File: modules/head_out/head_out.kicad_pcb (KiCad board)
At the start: 2 copper layers, 30.5 x 68.6 mm, 28 parts, among them U1 MCP6002-xSN

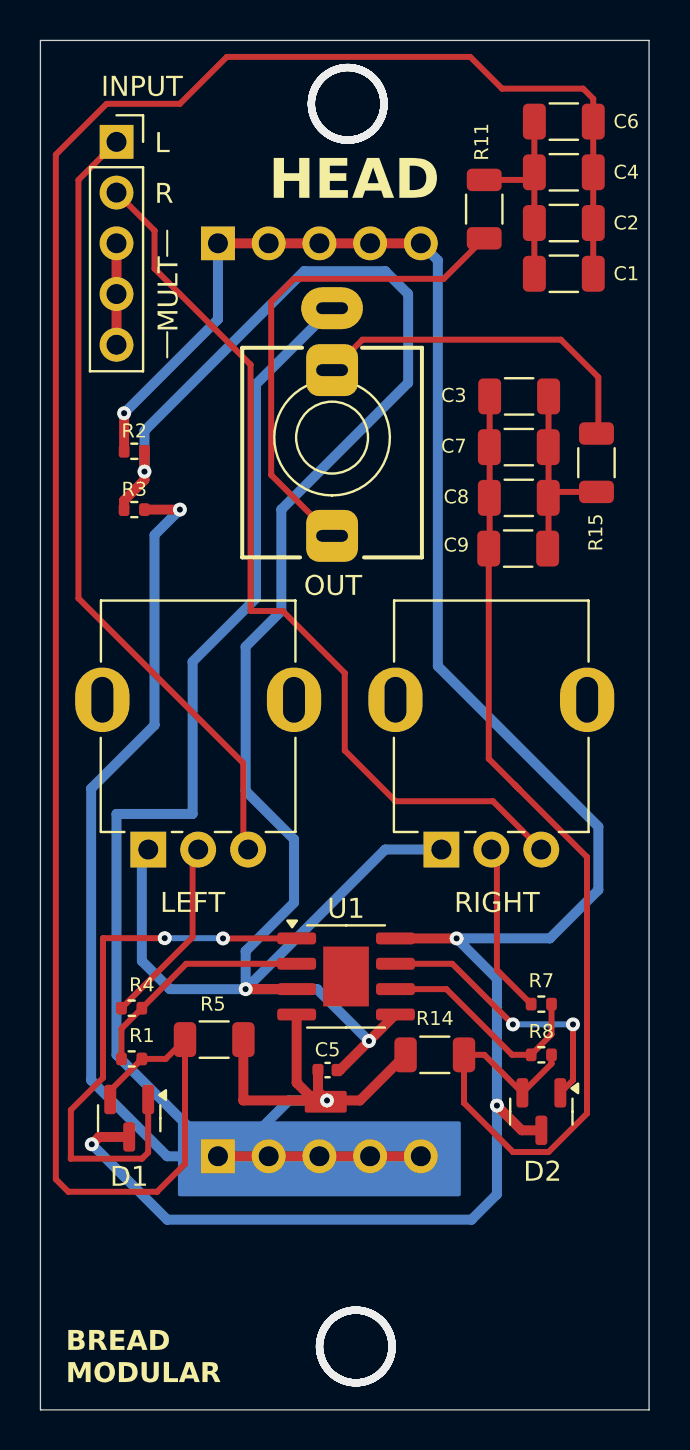
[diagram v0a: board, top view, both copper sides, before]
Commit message: head_out: Add more volume to support larger headphones. Now we offer more volume and removed the transistor. The opamp can handle the power requirment decently.
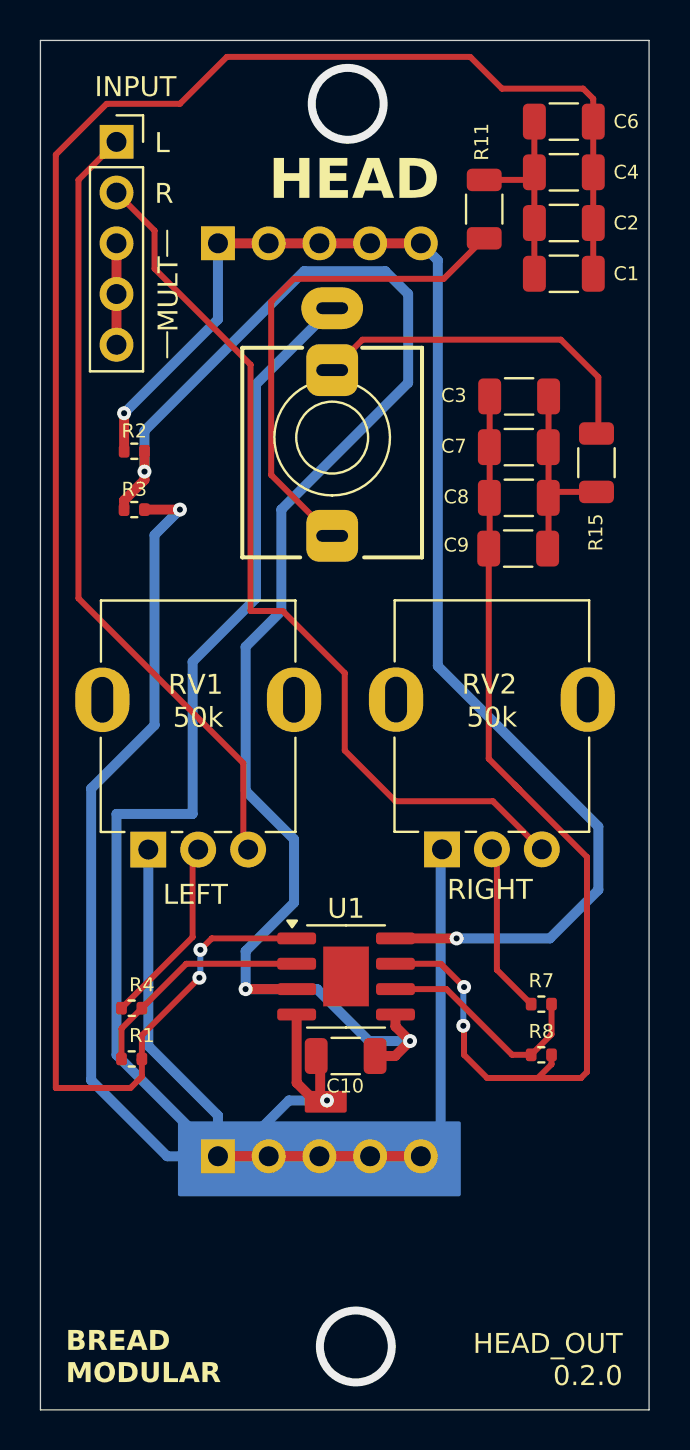
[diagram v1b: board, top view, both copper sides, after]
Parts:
- removed C5: 0.1uf, Capacitor_SMD:C_0402_1005Metric
- removed D1, D2: SS8050, Package_TO_SOT_SMD:SOT-23
- removed INPUT: Conn_01x05_Socket, Connector_PinSocket_2.54mm:PinSocket_1x05_P2.54mm_Vertical
- removed LEFT, RIGHT: 50k, BreadModular_Pots:Potentiometer_RV09
- removed OUT: AudioJack3, BreadModular_AudioJacks:Jack_3.5mm_QingPu_WQP-PJ366ST_Vertical
- removed R14, R5: 100, Resistor_SMD:R_1206_3216Metric
- added C10: 100uf, Capacitor_SMD:C_1206_3216Metric, F.Cu at (62.3, 91.5)
- added INPUT1: Conn_01x05_Socket, Connector_PinSocket_2.54mm:PinSocket_1x05_P2.54mm_Vertical, F.Cu at (50.8, 45.7)
- added J1: AudioJack3, BreadModular_AudioJacks:Jack_3.5mm_QingPu_WQP-PJ366ST_Vertical, F.Cu at (61.6, 60.5)
- added RV1: 50k, BreadModular_Pots:Potentiometer_RV09, F.Cu at (55.0, 74.2)
- added RV2: 50k, BreadModular_Pots:Potentiometer_RV09, F.Cu at (69.7, 74.2)
- R1, R8: value 22k -> 100k
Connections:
- net +5V renamed V_SUPPLY
- U1 pad 1: Net-(D1-K-Pad1) -> Net-(C1-Pad1)
- U1 pad 7: Net-(D2-K-Pad1) -> Net-(C3-Pad1)
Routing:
- net V_SUPPLY: track 110.5 -> 69.8 mm, vias 4 -> 2
- net Net-(D1-K-Pad1): track 28.2 -> 0.00 mm, vias 2 -> 0
- net +2.5V: track 100.6 -> 77.9 mm
- net GND: track 127.3 -> 148.5 mm
- net Net-(D2-K-Pad1): track 13.9 -> 0.00 mm, vias 2 -> 0
- net Net-(C1-Pad1): track 108.9 -> 102.6 mm, vias 0 -> 2
- net Net-(C3-Pad1): track 54.7 -> 51.6 mm, vias 0 -> 2
- net (no net): vias 8 -> 2
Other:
- board text added: "HEAD_OUT 0.2.0"
- board text added: "INPUT"
- board text added: "LEFT"
- board text added: "RIGHT"

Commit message: head_out: Add left to right input normalling This is a passive implementation and it works pretty well.
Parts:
- added C5: 0.1uf, Capacitor_SMD:C_0402_1005Metric, F.Cu at (50.0, 65.8)
- added R9: 1M, Resistor_SMD:R_0402_1005Metric, F.Cu at (51.7, 59.0)
- added U2: MCP6002-xSN, Package_SO:SOIC-8-1EP_3.9x4.9mm_P1.27mm_EP2.29x3mm, F.Cu at (52.5, 62.2)
- moved R2 6.82 mm to (51.0, 68.0)
- moved R3 4.63 mm to (54.2, 68.0)
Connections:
- RV1 pad 3: IN_L -> Net-(U2A--)
- RV2 pad 3: IN_R -> Net-(U2B--)
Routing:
- net GND: track 148.5 -> 190.6 mm, vias 2 -> 3
- net Net-(U2A--): track 0.00 -> 31.4 mm, vias 0 -> 2
- net Net-(U2B--): track 0.00 -> 31.2 mm, vias 0 -> 2
- net IN_L: track 39.8 -> 19.3 mm
- net IN_R: track 45.5 -> 26.3 mm
- net V_SUPPLY: track 69.8 -> 84.3 mm, vias 2 -> 3
- net +2.5V: track 77.9 -> 87.8 mm
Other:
- board text added: "HEAD_OUT 0.3.0"
- board text removed: "HEAD_OUT 0.2.0"

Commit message: head_out: Add input normalizing
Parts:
- added R5: 100k, Resistor_SMD:R_0402_1005Metric, F.Cu at (55.4, 54.6)
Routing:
- net IN_L: track 19.3 -> 30.4 mm
- net GND: track 190.6 -> 198.0 mm, vias 3 -> 4
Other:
- board text added: "HEAD_OUT 0.4.0"
- board text removed: "HEAD_OUT 0.3.0"

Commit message: head_out_1.0.0
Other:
- board text added: "HEAD_OUT 1.0.0"
- board text removed: "HEAD_OUT 0.4.0"
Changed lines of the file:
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@@
 		)
 	)
-	(gr_text "HEAD_OUT\n0.4.0"
+	(gr_text "HEAD_OUT\n1.0.0"
 		(at 76.15 108.1 0)
 		(layer "F.SilkS")
